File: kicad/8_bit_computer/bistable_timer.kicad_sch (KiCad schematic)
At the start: 9 parts, among them U1 NE555P

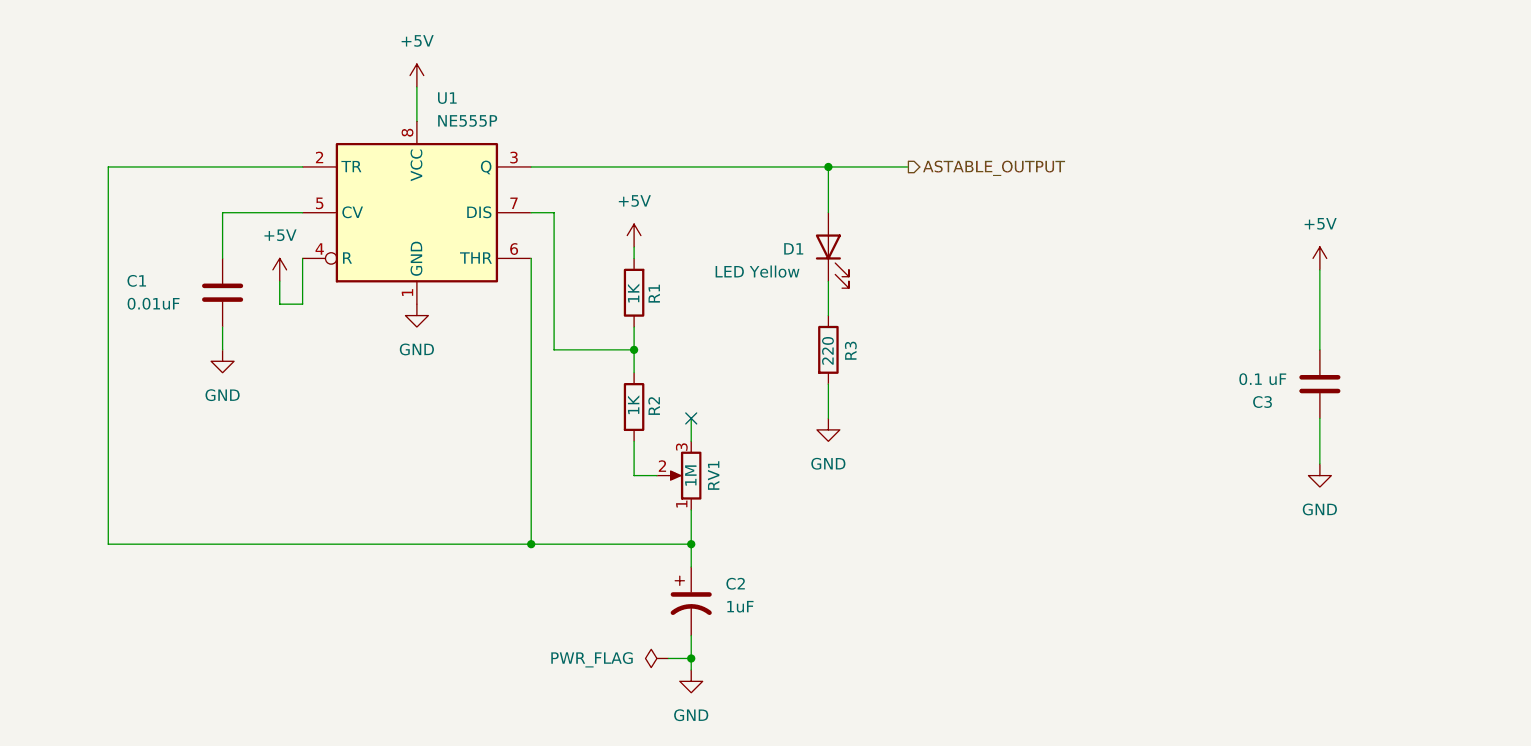
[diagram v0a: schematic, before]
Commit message: Bistable and Monstable Clocks
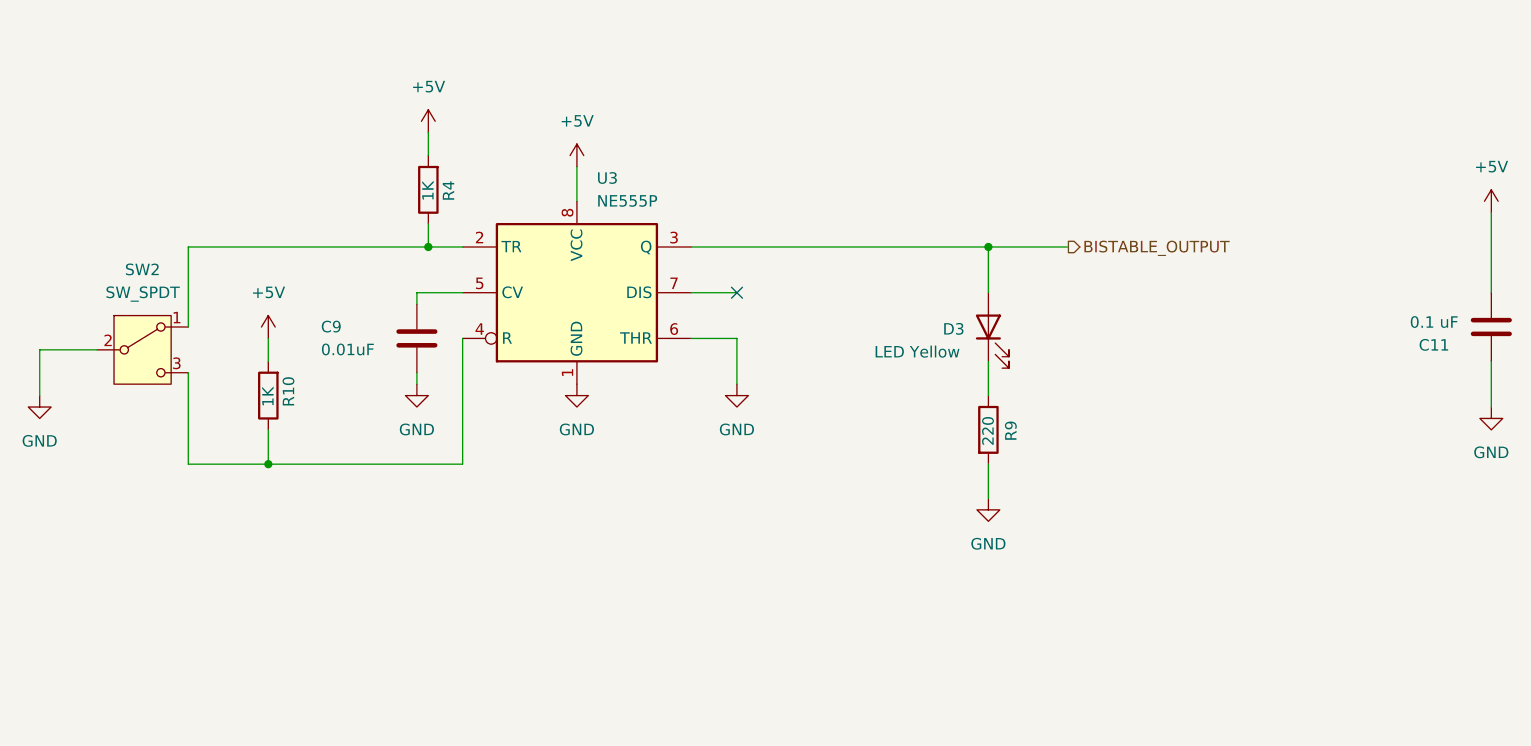
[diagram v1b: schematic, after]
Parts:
- removed C1: 0.01uF, Capacitor_THT:C_Disc_D5.0mm_W2.5mm_P2.50mm, symbol Device:C
- removed C2: 1uF, Capacitor_THT:CP_Radial_D5.0mm_P2.00mm, symbol Device:C_Polarized_US
- removed C3: 0.1 uF, Capacitor_THT:C_Disc_D5.0mm_W2.5mm_P2.50mm, symbol Device:C
- removed D1: LED Yellow, LED_THT:LED_D5.0mm, symbol Device:LED
- removed R1, R2: 1K, Resistor_THT:R_Axial_DIN0207_L6.3mm_D2.5mm_P7.62mm_Horizontal, symbol Device:R
- removed R3: 220, Resistor_THT:R_Axial_DIN0207_L6.3mm_D2.5mm_P7.62mm_Horizontal, symbol Device:R
- removed RV1: 1M, 8-bit-computer-custom-footprints:Potentiometer_CT-6EP105, symbol Device:R_Potentiometer
- removed U1: NE555P, Package_DIP:DIP-8_W7.62mm, symbol Timer:NE555P
- added C11: 0.1 uF, Capacitor_THT:C_Disc_D5.0mm_W2.5mm_P2.50mm, symbol Device:C
- added C9: 0.01uF, Capacitor_THT:C_Disc_D5.0mm_W2.5mm_P2.50mm, symbol Device:C
- added D3: LED Yellow, LED_THT:LED_D5.0mm, symbol Device:LED
- added R10, R4: 1K, Resistor_THT:R_Axial_DIN0207_L6.3mm_D2.5mm_P7.62mm_Horizontal, symbol Device:R
- added R9: 220, Resistor_THT:R_Axial_DIN0207_L6.3mm_D2.5mm_P7.62mm_Horizontal, symbol Device:R
- added SW2: SW_SPDT, Button_Switch_THT:SW_Slide_SPDT_Straight_CK_OS102011MS2Q, symbol Switch:SW_SPDT
- added U3: NE555P, Package_DIP:DIP-8_W7.62mm, symbol Timer:NE555P
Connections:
- net +5V: now also C11.2, R10.2, R4.2, U3.8 (VCC)
- net GND: now also C11.1, C9.2, R9.2, SW2.2 (B), U3.1 (GND), U3.6 (THR)
- new net: D3.1 (K), R9.1
- new net: R4.1, SW2.1 (A), U3.2 (TR)
- new net: R10.1, SW2.3 (C), U3.4 (R)
- new net: C9.1, U3.5 (CV)
- new net BISTABLE_OUTPUT: D3.2 (A), U3.3 (Q)
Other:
- title: Astable Timer -> (none)

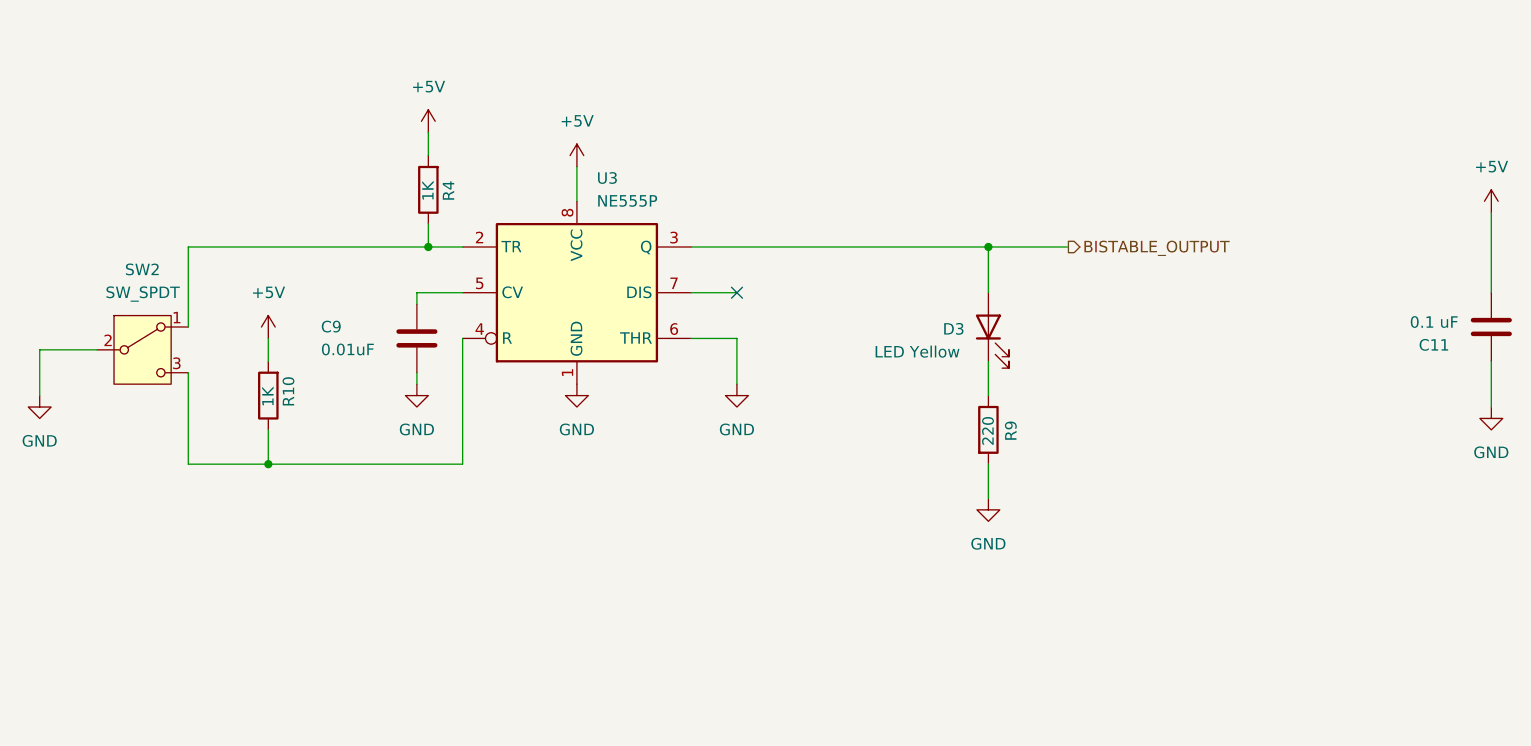
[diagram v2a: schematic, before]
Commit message: Mostly implemented register, still ERC errors
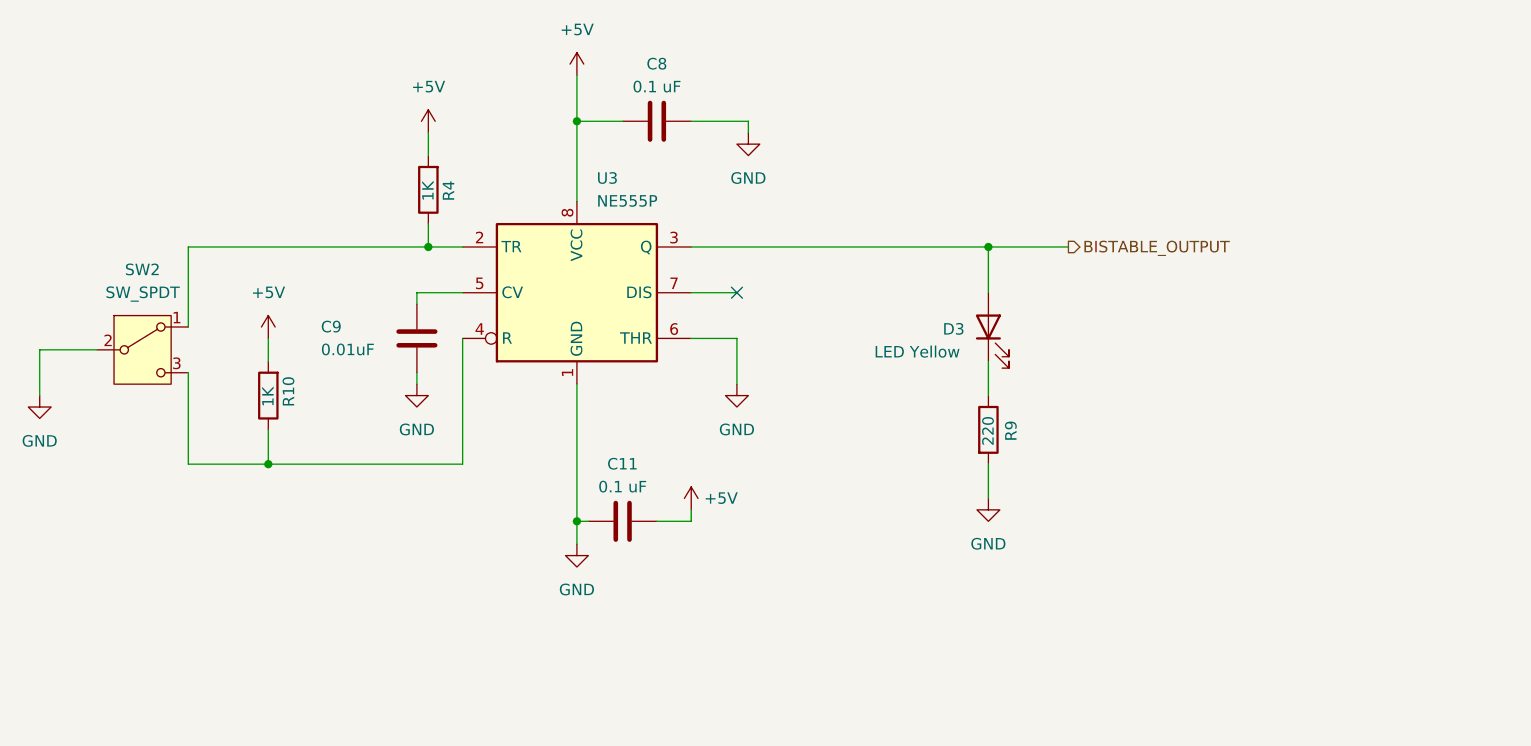
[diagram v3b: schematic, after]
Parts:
- added C8: 0.1 uF, Capacitor_THT:C_Disc_D5.0mm_W2.5mm_P2.50mm, symbol Device:C
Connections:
- net +5V: now also C8.1
- net GND: now also C8.2

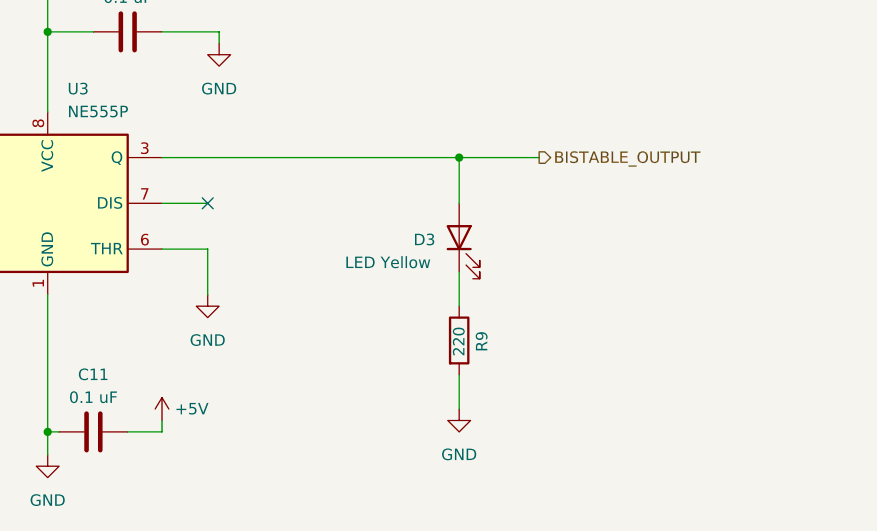
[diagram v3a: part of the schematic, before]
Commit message: Add pull up/down resistors to all vcc/gnd shorts
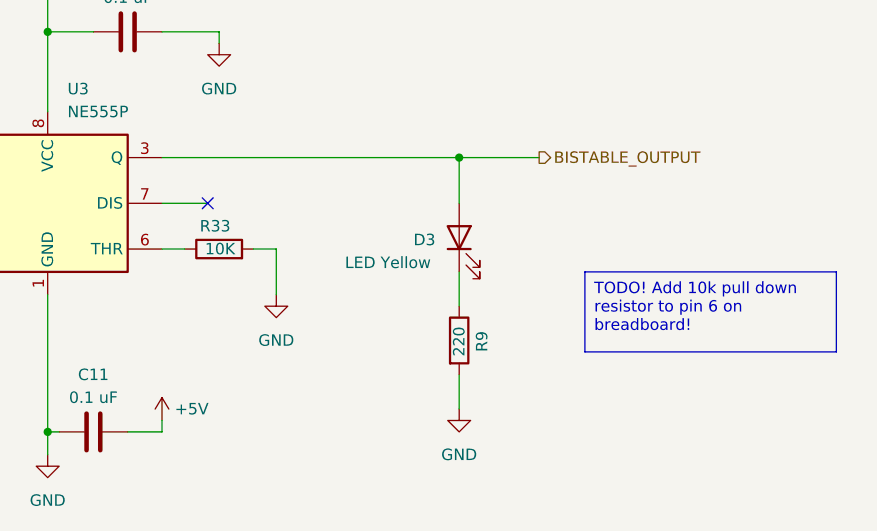
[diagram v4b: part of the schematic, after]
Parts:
- added R33: 10K, Resistor_THT:R_Axial_DIN0207_L6.3mm_D2.5mm_P7.62mm_Horizontal, symbol Device:R
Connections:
- net GND: now also R33.2; no longer U3.6 (THR)
- new net: R33.1, U3.6 (THR)
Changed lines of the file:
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@@
 	(wire
 		(pts
-			(xy 135.89 93.98) (xy 140.97 93.98)
+			(xy 148.59 93.98) (xy 146.05 93.98)
 		)
 		(stroke
@@
 	(wire
 		(pts
-			(xy 140.97 93.98) (xy 140.97 99.06)
-		)
-		(stroke
-			(width 0)
-			(type default)
-		)
-	)
-	(wire
-		(pts
 			(xy 135.89 114.3) (xy 135.89 113.03)
 		)
@@
 	(wire
 		(pts
+			(xy 135.89 93.98) (xy 138.43 93.98)
+		)
+		(stroke
+			(width 0)
+			(type default)
+		)
+	)
+	(wire
+		(pts
 			(xy 168.91 107.95) (xy 168.91 111.76)
 		)
@@
 	(wire
 		(pts
+			(xy 148.59 93.98) (xy 148.59 99.06)
+		)
+		(stroke
+			(width 0)
+			(type default)
+		)
+	)
+	(wire
+		(pts
 			(xy 88.9 93.98) (xy 88.9 96.52)
 		)
@@
 			(width 0)
 			(type default)
+		)
+	)
+	(text_box "TODO! Add 10k pull down resistor to pin 6 on breadboard!"
+		(exclude_from_sim no)
+		(at 182.88 96.52 0)
+		(size 27.94 8.89)
+		(stroke
+			(width 0)
+			(type default)
+		)
+		(fill
+			(type none)
+		)
+		(effects
+			(font
+				(size 1.27 1.27)
+			)
+			(justify left top)
 		)
 	)
@@
 	(symbol
 		(lib_id "power:GND")
-		(at 140.97 99.06 0)
+		(at 148.59 99.06 0)
 		(unit 1)
 		(exclude_from_sim no)
@@
 		(fields_autoplaced yes)
 		(property "Reference" "#PWR028"
-			(at 140.97 105.41 0)
+			(at 148.59 105.41 0)
 			(effects
 				(font
@@
 		)
 		(property "Value" "GND"
-			(at 140.97 104.14 0)
+			(at 148.59 104.14 0)
 			(effects
 				(font
@@
 		)
 		(property "Footprint" ""
-			(at 140.97 99.06 0)
+			(at 148.59 99.06 0)
 			(effects
 				(font
@@
 		)
 		(property "Datasheet" ""
-			(at 140.97 99.06 0)
+			(at 148.59 99.06 0)
 			(effects
 				(font
@@
 		)
 		(property "Description" "Power symbol creates a global label with name \"GND\" , ground"
-			(at 140.97 99.06 0)
+			(at 148.59 99.06 0)
 			(effects
 				(font
@@
 					(unit 1)
 				)
+			)
+		)
+	)
+	(symbol
+		(lib_id "Device:R")
+		(at 142.24 93.98 90)
+		(unit 1)
+		(exclude_from_sim no)
+		(in_bom yes)
+		(on_board yes)
+		(dnp no)
+		(property "Reference" "R33"
+			(at 143.51 91.44 90)
+			(effects
+				(font
+					(size 1.27 1.27)
+				)
+				(justify left)
+			)
+		)
+		(property "Value" "10K"
+			(at 144.018 93.98 90)
+			(effects
+				(font
+					(size 1.27 1.27)
+				)
+				(justify left)
+			)
+		)
+		(property "Footprint" "Resistor_THT:R_Axial_DIN0207_L6.3mm_D2.5mm_P7.62mm_Horizontal"
+			(at 142.24 95.758 90)
+			(effects
+				(font
+					(size 1.27 1.27)
+				)
+				(hide yes)
+			)
+		)
+		(property "Datasheet" "https://www.yageo.com/upload/media/product/app/datasheet/lr/yageo-mfr_datasheet.pdf"
+			(at 142.24 93.98 0)
+			(effects
+				(font
+					(size 1.27 1.27)
+				)
+				(hide yes)
+			)
+		)
+		(property "Description" "Resistor"
+			(at 142.24 93.98 0)
+			(effects
+				(font
+					(size 1.27 1.27)
+				)
+				(hide yes)
+			)
+		)
+		(property "Digkey PN" "13-MFR-25FRF52-10KCT-ND "
+			(at 142.24 93.98 0)
+			(effects
+				(font
+					(size 1.27 1.27)
+				)
+				(hide yes)
+			)
+		)
+		(property "Manufacturer PN" "MFR-25FRF52-10K"
+			(at 142.24 93.98 0)
+			(effects
+				(font
+					(size 1.27 1.27)
+				)
+				(hide yes)
+			)
+		)
+		(property "DigiKey URL" "https://www.digikey.com/en/products/detail/yageo/MFR-25FRF52-10K/14626"
+			(at 142.24 93.98 0)
+			(effects
+				(font
+					(size 1.27 1.27)
+				)
+				(hide yes)
+			)
+		)
+		(property "Price" "0.10"
+			(at 142.24 93.98 0)
+			(effects
+				(font
+					(size 1.27 1.27)
+				)
+				(hide yes)
+			)
+		)
+		(property "DigiKey PN" ""
+			(at 142.24 93.98 0)
+			(effects
+				(font
+					(size 1.27 1.27)
+				)
+				(hide yes)
+			)
+		)
+		(pin "2"
+		)
+		(pin "1"
+		)
+		(instances
+			(project "8_bit_computer"
+				(path "/24dbb59b-fc31-4588-b2ee-d18f20639e07/62eb35ce-6b42-428c-8bc5-4f1b242b0bef/574038bf-e5a4-4395-a0a6-883cc4308fec"
+					(reference "R33")
+					(unit 1)
+				)
